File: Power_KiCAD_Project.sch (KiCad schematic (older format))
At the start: 22 parts

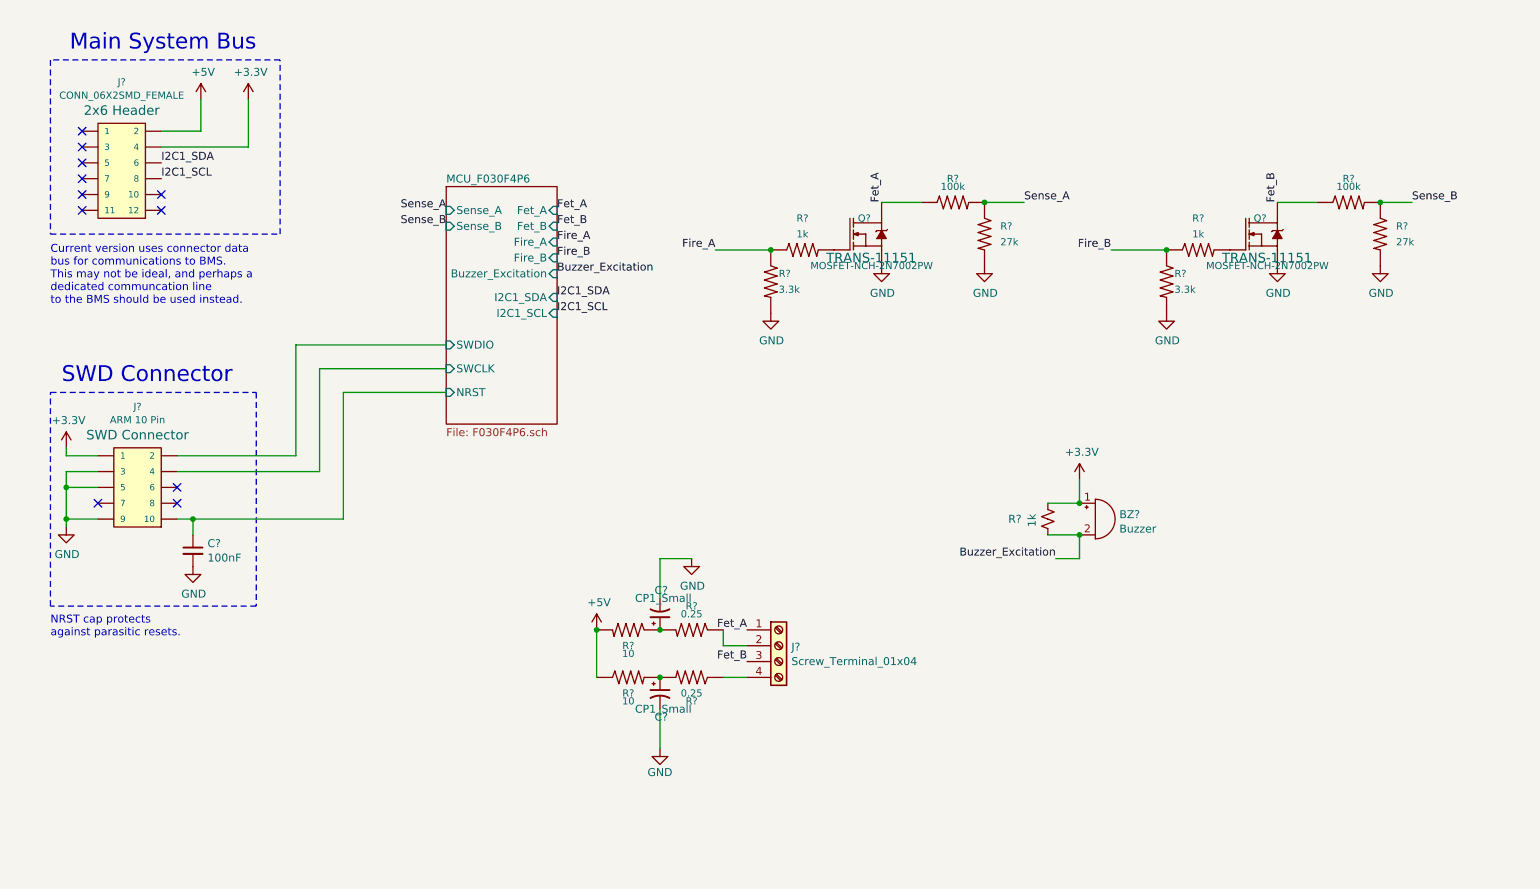
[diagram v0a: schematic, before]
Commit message: Board update
Added capacitors and extra charge stuff
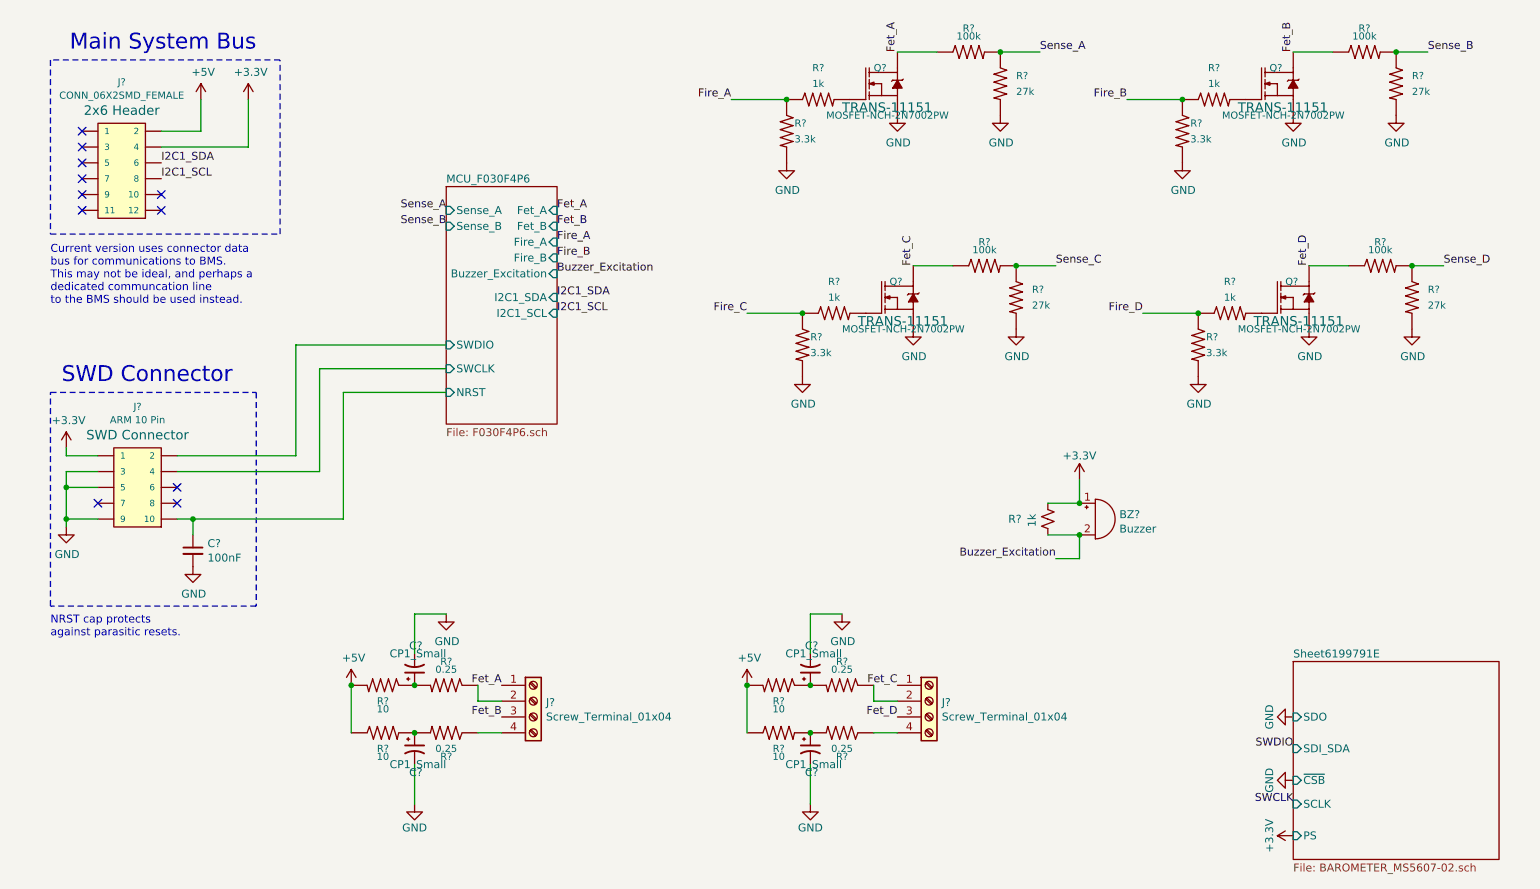
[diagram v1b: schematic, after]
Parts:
- added C? (x2): CP1_Small, symbol Device:CP1_Small
- added J?: Screw_Terminal_01x04, symbol Connector:Screw_Terminal_01x04
- added Q? (x2): MOSFET-NCH-2N7002PW, SOT323, symbol SparkFun-DiscreteSemi:MOSFET-NCH-2N7002PW
- added R? (x2): 0.25, 0402, symbol SparkFun-Resistors:RESISTOR0402
- added R? (x2): 10, 0402, symbol SparkFun-Resistors:RESISTOR0402
- added R? (x2): 1k, 0402, symbol SparkFun-Resistors:RESISTOR0402
- added R? (x2): 3.3k, 0402, symbol SparkFun-Resistors:RESISTOR0402
- added R? (x2): 100k, 0402, symbol SparkFun-Resistors:RESISTOR0402
- added R? (x2): 27k, 0402, symbol SparkFun-Resistors:RESISTOR0402
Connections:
- net +5V: now also R?.1, R?.2
- net GND: now also C?.2, C?.2, Q?.2 (S), Q?.2 (S), R?.2, R?.2, R?.2, R?.2
- new net: J?.2 (Pin_2), R?.1
- new net: J?.4 (Pin_4), R?.1
- new net: C?.1, R?.2, R?.2
- new net: C?.1, R?.1, R?.2
- new net: Q?.1 (G), R?.2 (x2)
- new net Fet_C: J?.1 (Pin_1), Q?.3 (D), R?.1
- new net Fet_D: J?.3 (Pin_3), Q?.3 (D), R?.1
- new net Fire_C: R?.1, R?.1
- new net Fire_D: R?.1, R?.1
- new net Sense_C: R?.1, R?.2
- new net Sense_D: R?.1, R?.2
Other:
- moved on the sheet: C?, J?, Q?, R?

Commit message: Edit to bus
Bus changed as well as some other things to almost finish it up
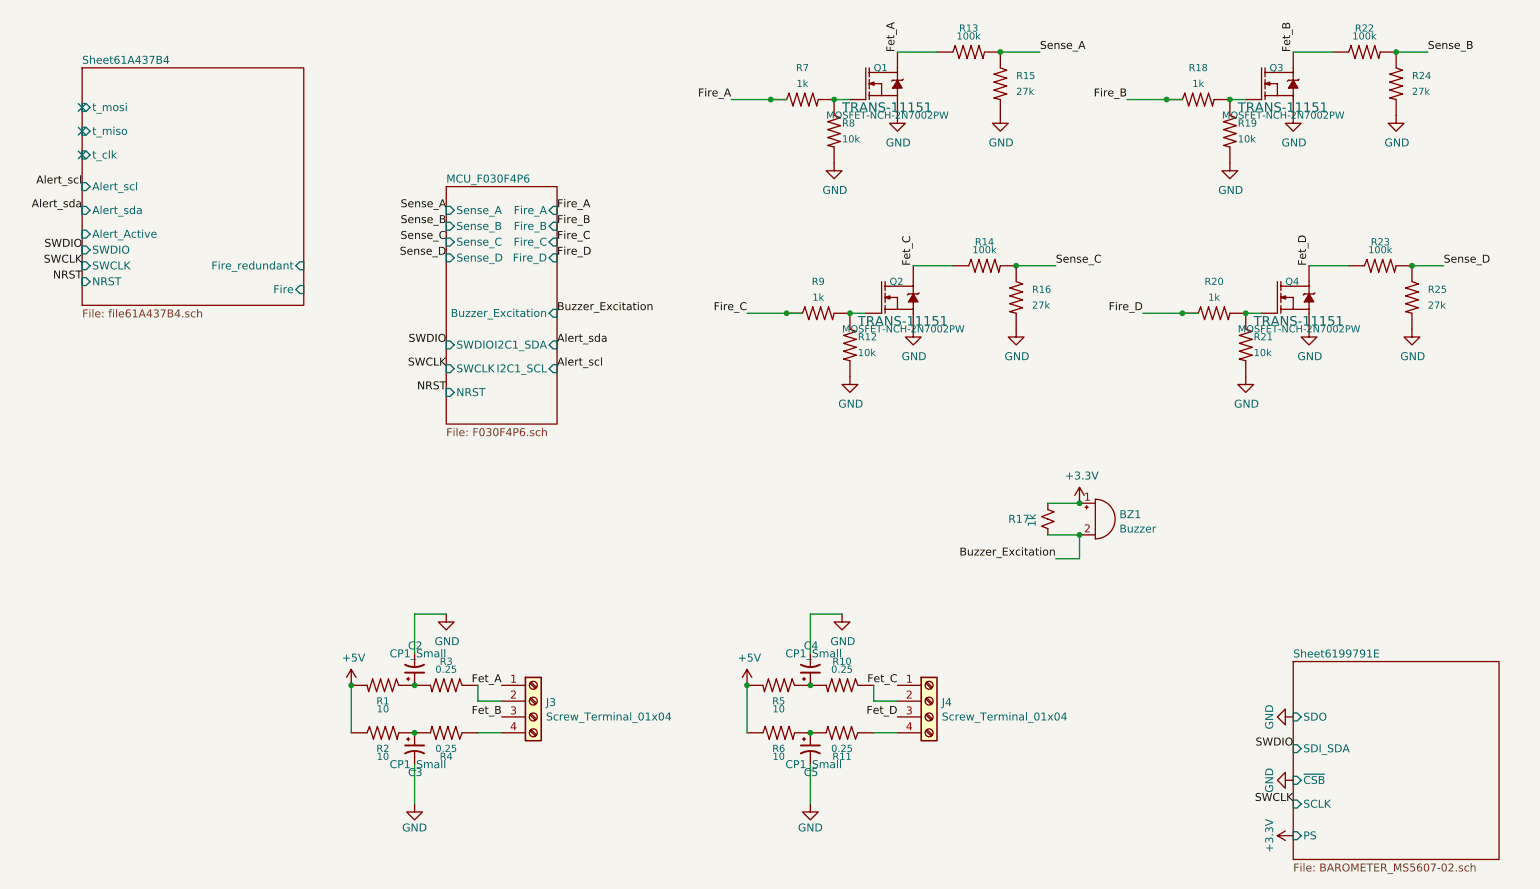
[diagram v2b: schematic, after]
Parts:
- removed C?: 100nF, symbol Device:C_Small
- removed J?: ARM 10 Pin, 2X5-RA, symbol SparkFun-Connectors:CONN_05X2RA
- removed J?: CONN_06X2SMD_FEMALE, 2X6_SMD, symbol SparkFun-Connectors:CONN_06X2SMD_FEMALE
- R1, R10, R11, R13, R14, R15, R16, R18, R2, R20, R22, R23, R24, R25, R3, R4, R5, R6, R7, R9: renamed from R?; footprint 0402 -> Resistor_SMD:R_0603_1608Metric
- R12, R19, R21, R8: renamed from R?; value 3.3k -> 10k; footprint 0402 -> Resistor_SMD:R_0603_1608Metric
- R17: renamed from R?; footprint (none) -> Resistor_SMD:R_0603_1608Metric
- gave numbers to parts that had none: 11
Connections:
- net labels added: Alert_scl, Alert_sda, NRST
- net labels removed: I2C1_SCL, I2C1_SDA
- wire segments 54 -> 38
- no-connect marks 11 -> 3
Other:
- note removed: "Current version uses connector data\nbus for communications to BMS.\nThis may not be ideal, and perhaps a \ndedicated communcation line\nto the BMS should be used instead."
- note removed: "Main System Bus"
- note removed: "NRST cap protects\nagainst parasitic resets."
- note removed: "SWD Connector"
- moved on the sheet: R12, R18, R19, R20, R21, R7, R8, R9
